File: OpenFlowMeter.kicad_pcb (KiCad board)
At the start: 2 copper layers, 74.5 x 28 mm, 101 parts, among them J1 Screw_Terminal_01x02, J2 Screw_Terminal_01x02, J3 Conn_01x06, J4 Conn_02x03_Odd_Even, J5 Conn_01x03, J6 Conn_02x04_Odd_Even, J7 Conn_02x03_Odd_Even, Q1 BC856, Q2 BC856, U1 LT1492, U2 STM32F103C8Tx, U3 LT1492, U4 R-78C3.3-1.0, U5 SN65HVD231, U6 LT1492, U7 24LC64, Y1 12 MHz

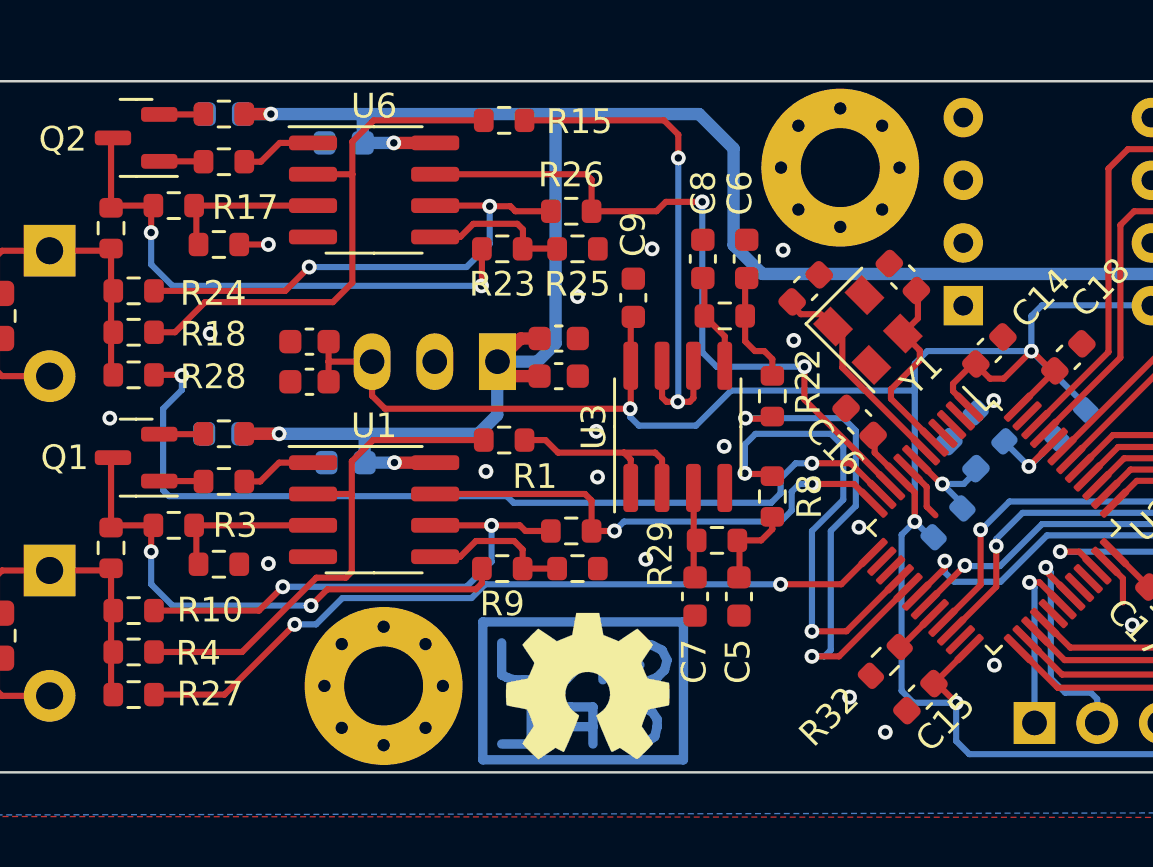
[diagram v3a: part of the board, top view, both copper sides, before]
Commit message: added ADC protection
added Zener diodes as ADC input protection in combination with current limiting resistors.
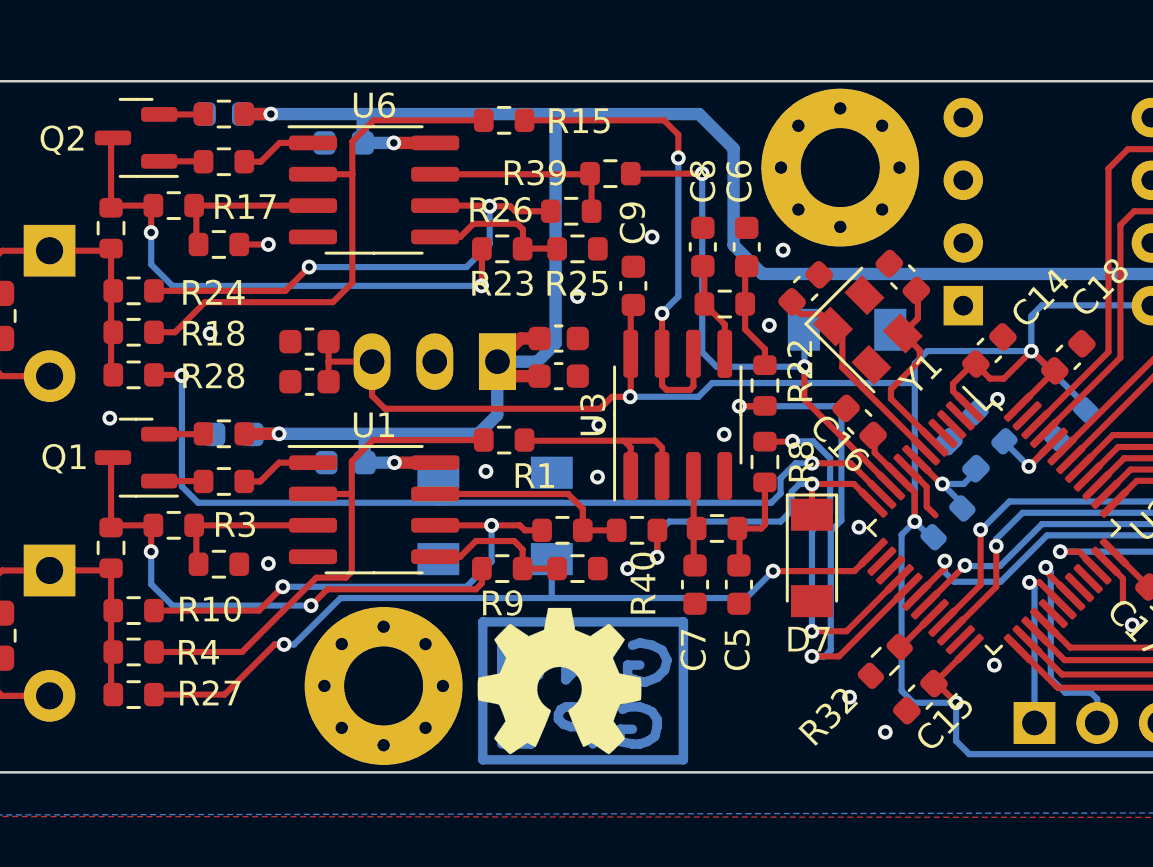
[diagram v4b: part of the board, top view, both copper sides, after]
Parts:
- added D5: 3V3, Diode_SMD:D_MiniMELF, B.Cu at (152.9, 92.8)
- added D6: 3V3, Diode_SMD:D_MiniMELF, B.Cu at (136.3, 100.4)
- added D7: 3V3, Diode_SMD:D_MiniMELF, F.Cu at (151.5, 102.1)
- added D8: 3V3, Diode_SMD:D_MiniMELF, B.Cu at (140.9, 100.4)
- added R39: 1k, Resistor_SMD:R_0603_1608Metric, F.Cu at (143.3, 86.5)
- added R40: 1k, Resistor_SMD:R_0603_1608Metric, F.Cu at (144.4, 101.0)
- C5, C6, C7, C8, C9: value C -> 100n
- moved R8 1.43 mm to (149.6, 98.2)
- moved REF** 1.16 mm to (141.3, 107.1)
- moved R22 0.53 mm to (149.6, 95.1)
- moved C6 0.48 mm to (148.8, 89.5)
- moved C8 0.48 mm to (147.1, 89.5)
- moved C9 0.48 mm to (144.2, 91.1)
- moved R30 0.48 mm to (148.0, 91.8)
- moved U3 0.48 mm to (146.1, 96.3)
- moved C5 0.48 mm to (148.5, 103.2)
- moved C7 0.48 mm to (146.8, 103.2)
- moved R29 0.48 mm to (147.6, 100.9)
- moved C1 0.41 mm to (128.0, 97.1)
- moved R12 0.36 mm to (141.4, 101.0)
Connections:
- R12 pad 1: /I1 -> Net-(R12-Pad1)
- R26 pad 1: /I2 -> Net-(R26-Pad1)
- U1 pad 7: /I1 -> Net-(R12-Pad1)
- U6 pad 7: /I2 -> Net-(R26-Pad1)
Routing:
- net Net-(R12-Pad1): track 0.00 -> 8.48 mm
- net Net-(R26-Pad1): track 0.00 -> 7.40 mm
- net /I1: track 20.6 -> 13.7 mm
- net /I2: track 29.1 -> 22.3 mm
- net /PWM1: track 19.1 -> 14.7 mm
- net /ISET 2: track 21.3 -> 19.6 mm
- net /U1: track 31.4 -> 33.0 mm
- net Net-(C5-Pad1): track 3.66 -> 4.45 mm
- net +3V3: track 160.6 -> 159.9 mm
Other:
- board text added: "Open FlowMeter"
- board text added: "v1.0"
- board text removed: "OpenFlowMeter"

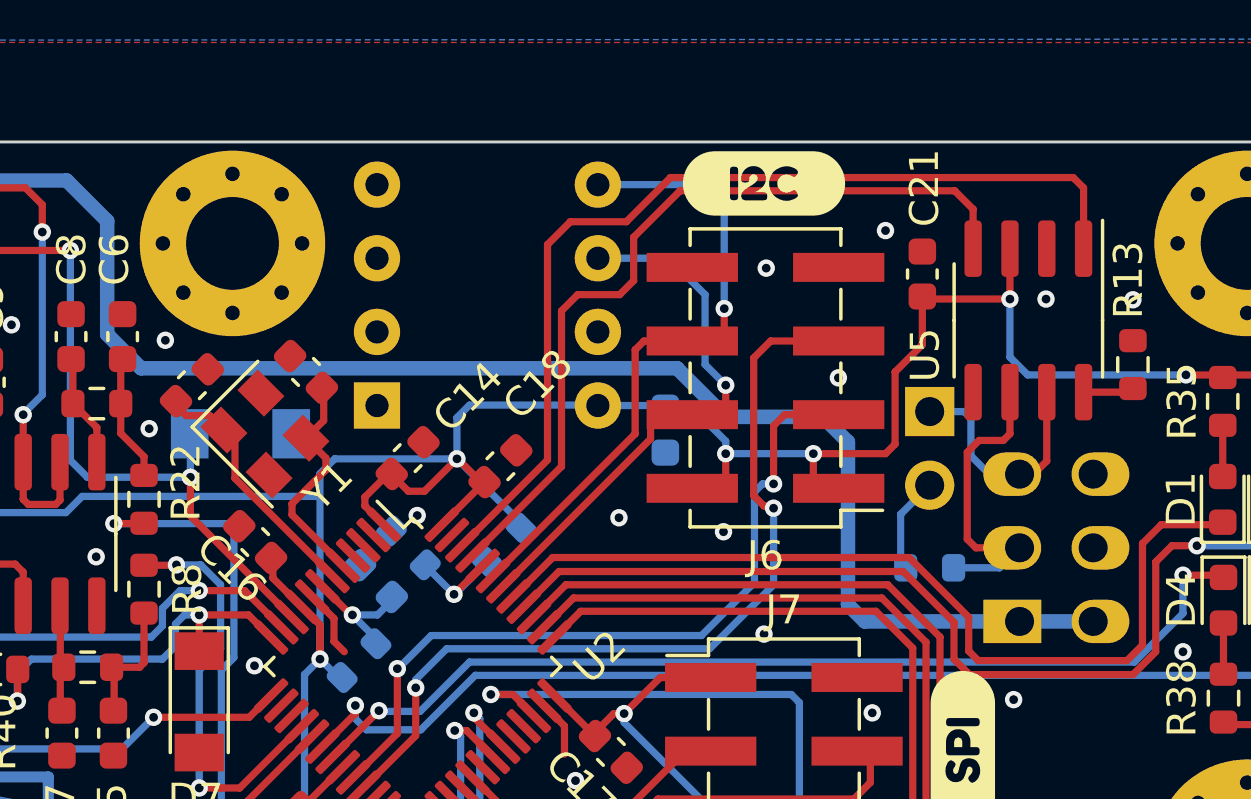
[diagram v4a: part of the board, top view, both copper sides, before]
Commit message: added write protection to EEPROM
added jumper, which can be opened and then the EEPROM is write protected.
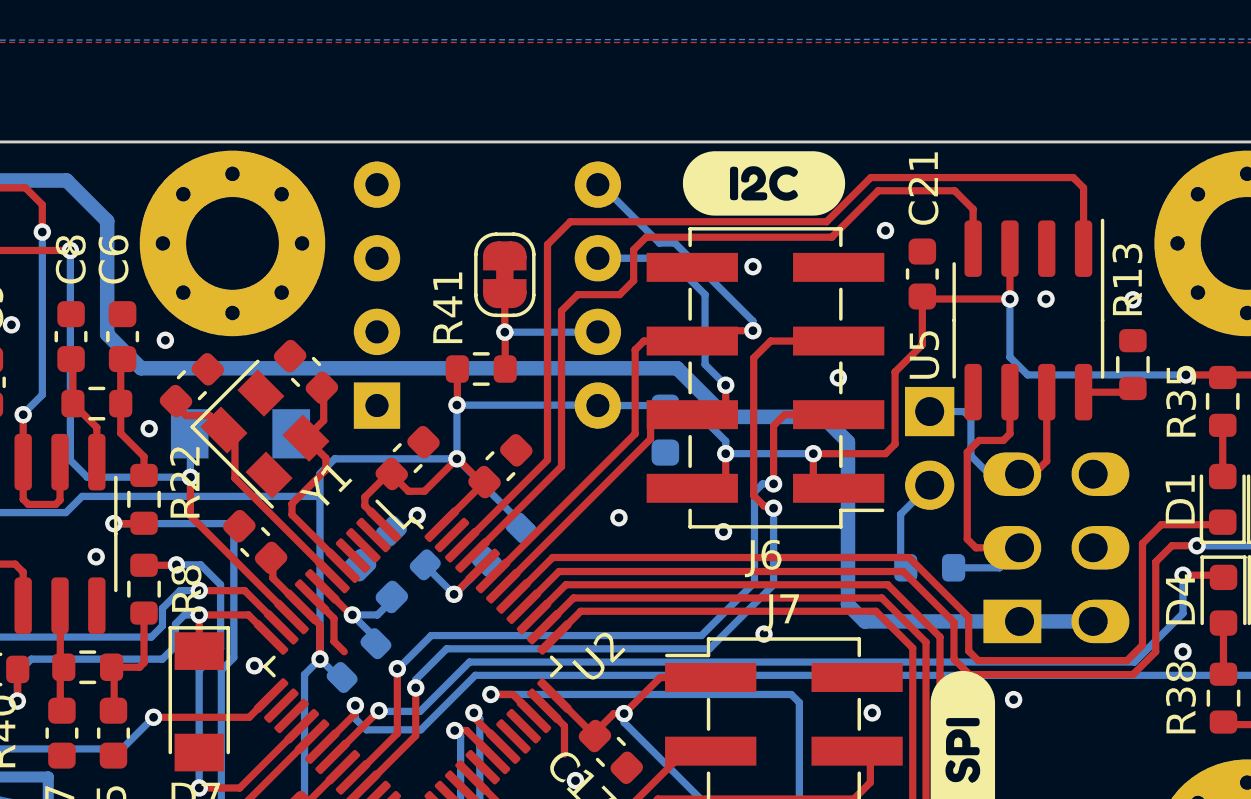
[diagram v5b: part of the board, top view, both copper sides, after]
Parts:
- added JP2: Jumper_2_Bridged, Jumper:SolderJumper-2_P1.3mm_Bridged_RoundedPad1.0x1.5mm, F.Cu at (162.0, 87.4)
- added R41: 10k, Resistor_SMD:R_0603_1608Metric, F.Cu at (161.2, 90.6)
- C1, C2, C3, C4: value C -> 100n
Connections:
- U7 pad 7: GND -> Net-(JP2-Pad2)
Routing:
- net Net-(JP2-Pad2): track 0.00 -> 5.75 mm, vias 0 -> 1
- net +3V3: track 159.9 -> 161.4 mm, vias 11 -> 12

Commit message: Some minor cleanups
Removed DRCs and did some minor cleanups.
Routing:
- net GND: vias 30 -> 39
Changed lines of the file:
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@@
   (segment (start 161.974109 98.096845) (end 167.0582 93.012754) (width 0.25) (layer "F.Cu") (net 28))
   (via (at 169.649 91.1606) (size 0.6) (drill 0.3) (layers "F.Cu" "B.Cu") (net 28))
-  (segment (start 169.649 91.1606) (end 168.9378 90.4494) (width 0.25) (layer "B.Cu") (net 28))
-  (segment (start 168.9378 88.0364) (end 167.6832 86.7818) (width 0.25) (layer "B.Cu") (net 28))
+  (segment (start 168.252 87.3506) (end 167.6832 86.7818) (width 0.25) (layer "B.Cu") (net 28))
   (segment (start 167.6832 86.7818) (end 165.2394 86.7818) (width 0.25) (layer "B.Cu") (net 28))
-  (segment (start 168.9378 90.4494) (end 168.9378 88.0364) (width 0.25) (layer "B.Cu") (net 28))
+  (segment (start 169.649 91.1606) (end 168.252 89.7636) (width 0.25) (layer "B.Cu") (net 28))
+  (segment (start 168.252 89.7636) (end 168.252 87.3506) (width 0.25) (layer "B.Cu") (net 28))
   (segment (start 155.733891 98.098891) (end 156.7204 99.0854) (width 0.25) (layer "F.Cu") (net 29))
   (segment (start 156.7204 99.0854) (end 156.7712 99.0854) (width 0.25) (layer "F.Cu") (net 29))
@@
   (segment (start 161.013 101.1682) (end 188.8006 101.1682) (width 0.25) (layer "B.Cu") (net 30))
   (segment (start 156.8728 102.2096) (end 156.8728 102.6668) (width 0.25) (layer "B.Cu") (net 30))
+  (segment (start 169.649 89.2048) (end 169.2172 89.6366) (width 0.25) (layer "F.Cu") (net 33))
   (segment (start 161.620555 97.741245) (end 166.5248 92.837) (width 0.25) (layer "F.Cu") (net 33))
   (segment (start 166.5248 89.9414) (end 166.8296 89.6366) (width 0.25) (layer "F.Cu") (net 33))
   (segment (start 166.5248 92.837) (end 166.5248 89.9414) (width 0.25) (layer "F.Cu") (net 33))
   (segment (start 166.8296 89.6366) (end 168.4956 89.6366) (width 0.25) (layer "F.Cu") (net 33))
-  (segment (start 169.5728 89.281) (end 169.2172 89.6366) (width 0.25) (layer "F.Cu") (net 33))
-  (segment (start 170.5888 89.281) (end 169.5728 89.281) (width 0.25) (layer "F.Cu") (net 33))
-  (via (at 170.5888 89.281) (size 0.6) (drill 0.3) (layers "F.Cu" "B.Cu") (net 33))
-  (segment (start 170.5888 89.281) (end 170.5888 88.9508) (width 0.25) (layer "B.Cu") (net 33))
-  (segment (start 165.3464 84.2418) (end 165.2394 84.2418) (width 0.25) (layer "B.Cu") (net 33))
-  (segment (start 170.5888 88.9508) (end 167.8964 86.2584) (width 0.25) (layer "B.Cu") (net 33))
-  (segment (start 167.363 86.2584) (end 165.3464 84.2418) (width 0.25) (layer "B.Cu") (net 33))
-  (segment (start 167.8964 86.2584) (end 167.363 86.2584) (width 0.25) (layer "B.Cu") (net 33))
+  (segment (start 169.649 88.6714) (end 169.649 89.2048) (width 0.25) (layer "F.Cu") (net 33))
+  (via (at 169.649 88.6714) (size 0.6) (drill 0.3) (layers "F.Cu" "B.Cu") (net 33))
+  (segment (start 169.649 84.9884) (end 169.649 88.6714) (width 0.25) (layer "B.Cu") (net 33))
+  (segment (start 168.9024 84.2418) (end 169.649 84.9884) (width 0.25) (layer "B.Cu") (net 33))
+  (segment (start 165.2394 84.2418) (end 168.9024 84.2418) (width 0.25) (layer "B.Cu") (net 33))
   (segment (start 163.9848 88.5952) (end 164.5436 88.0364) (width 0.25) (layer "F.Cu") (net 34))
   (segment (start 166.474 87.5538) (end 166.474 86.487) (width 0.25) (layer "F.Cu") (net 34))
@@
   (segment (start 145.5936 95.2738) (end 146.5366 95.2738) (width 0.25) (layer "F.Cu") (net 37))
   (segment (start 146.074 84.9338) (end 145.4936 84.3534) (width 0.25) (layer "F.Cu") (net 37))
-  (segment (start 146.074 85.8774) (end 146.074 84.9338) (width 0.25) (layer "F.Cu") (net 37))
+  (segment (start 145.4936 84.3534) (end 139.8416 84.3534) (width 0.25) (layer "F.Cu") (net 37))
   (segment (start 145.5936 95.2738) (end 145.4155 95.0957) (width 0.25) (layer "F.Cu") (net 37))
   (segment (start 145.4155 95.0957) (end 145.4155 93.8148) (width 0.25) (layer "F.Cu") (net 37))
+  (segment (start 146.074 84.9884) (end 146.074 84.9338) (width 0.25) (layer "F.Cu") (net 37))
   (segment (start 146.5366 95.2738) (end 146.6855 95.1249) (width 0.25) (layer "F.Cu") (net 37))
   (segment (start 146.6855 95.1249) (end 146.6855 93.8148) (width 0.25) (layer "F.Cu") (net 37))
-  (segment (start 145.4936 84.3534) (end 139.8416 84.3534) (width 0.25) (layer "F.Cu") (net 37))
   (segment (start 145.4155 93.8148) (end 145.4155 92.1785) (width 0.25) (layer "F.Cu") (net 37))
   (via (at 145.4155 92.1785) (size 0.6) (drill 0.3) (layers "F.Cu" "B.Cu") (net 37))
-  (via (at 146.074 85.8774) (size 0.6) (drill 0.3) (layers "F.Cu" "B.Cu") (net 37))
-  (segment (start 145.4155 92.1531) (end 146.074 91.4946) (width 0.25) (layer "B.Cu") (net 37))
-  (segment (start 145.4155 92.1785) (end 145.4155 92.1531) (width 0.25) (layer "B.Cu") (net 37))
-  (segment (start 146.074 91.4946) (end 146.074 85.8774) (width 0.25) (layer "B.Cu") (net 37))
+  (via (at 146.074 84.9884) (size 0.6) (drill 0.3) (layers "F.Cu" "B.Cu") (net 37))
+  (segment (start 145.4155 92.1531) (end 145.4155 92.1785) (width 0.25) (layer "B.Cu") (net 37))
+  (segment (start 146.074 91.4946) (end 145.4155 92.1531) (width 0.25) (layer "B.Cu") (net 37))
+  (segment (start 146.074 84.9884) (end 146.074 91.4946) (width 0.25) (layer "B.Cu") (net 37))
   (segment (start 118.468 93.0383) (end 118.468 94.5134) (width 0.25) (layer "F.Cu") (net 40))
   (segment (start 118.468 94.5134) (end 118.6712 94.7166) (width 0.25) (layer "F.Cu") (net 40))
@@
   (via (at 169.5728 96.2152) (size 0.6) (drill 0.3) (layers "F.Cu" "B.Cu") (free) (net 40))
   (via (at 142.852 96.6978) (size 0.6) (drill 0.3) (layers "F.Cu" "B.Cu") (free) (net 40))
+  (via (at 134.216 99.2124) (size 0.6) (drill 0.3) (layers "F.Cu" "B.Cu") (free) (net 40))
+  (via (at 138.153 85.6234) (size 0.6) (drill 0.3) (layers "F.Cu" "B.Cu") (free) (net 40))
   (via (at 129.4662 89.3826) (size 0.6) (drill 0.3) (layers "F.Cu" "B.Cu") (net 40))
   (via (at 147.932 97.0788) (size 0.6) (drill 0.3) (layers "F.Cu" "B.Cu") (free) (net 40))
+  (via (at 171.554 90.9574) (size 0.6) (drill 0.3) (layers "F.Cu" "B.Cu") (free) (net 40))
   (via (at 138.28 98.5774) (size 0.6) (drill 0.3) (layers "F.Cu" "B.Cu") (free) (net 40))
   (via (at 179.5804 102.0064) (size 0.6) (drill 0.3) (layers "F.Cu" "B.Cu") (free) (net 40))
   (via (at 173.5352 90.9066) (size 0.6) (drill 0.3) (layers "F.Cu" "B.Cu") (free) (net 40))
+  (via (at 119.23 98.5774) (size 0.6) (drill 0.3) (layers "F.Cu" "B.Cu") (free) (net 40))
   (via (at 159.0064 95.6564) (size 0.6) (drill 0.3) (layers "F.Cu" "B.Cu") (free) (net 40))
   (via (at 154.4598 109.1438) (size 0.6) (drill 0.3) (layers "F.Cu" "B.Cu") (free) (net 40))
   (via (at 185.4224 100.3554) (size 0.6) (drill 0.3) (layers "F.Cu" "B.Cu") (free) (net 40))
   (via (at 158.8794 106.426) (size 0.6) (drill 0.3) (layers "F.Cu" "B.Cu") (free) (net 40))
-  (via (at 170.5888 87.0712) (size 0.6) (drill 0.3) (layers "F.Cu" "B.Cu") (free) (net 40))
-  (via (at 165.966 95.7326) (size 0.6) (drill 0.3) (layers "F.Cu" "B.Cu") (free) (net 40))
+  (via (at 171.046 87.0712) (size 0.6) (drill 0.3) (layers "F.Cu" "B.Cu") (free) (net 40))
+  (via (at 165.966 96.2152) (size 0.6) (drill 0.3) (layers "F.Cu" "B.Cu") (free) (net 40))
   (via (at 153.012 107.7214) (size 0.6) (drill 0.3) (layers "F.Cu" "B.Cu") (free) (net 40))
   (via (at 175.1608 85.8266) (size 0.6) (drill 0.3) (layers "F.Cu" "B.Cu") (free) (net 40))
   (via (at 127.104 92.9894) (size 0.6) (drill 0.3) (layers "F.Cu" "B.Cu") (free) (net 40))
+  (via (at 134.216 102.0064) (size 0.6) (drill 0.3) (layers "F.Cu" "B.Cu") (free) (net 40))
   (via (at 142.8012 98.806) (size 0.6) (drill 0.3) (layers "F.Cu" "B.Cu") (free) (net 40))
+  (via (at 134.089 86.5124) (size 0.6) (drill 0.3) (layers "F.Cu" "B.Cu") (free) (net 40))
   (via (at 149.7608 92.6592) (size 0.6) (drill 0.3) (layers "F.Cu" "B.Cu") (free) (net 40))
   (via (at 170.9698 99.7458) (size 0.6) (drill 0.3) (layers "F.Cu" "B.Cu") (free) (net 40))
@@
   (via (at 153.393 100.838) (size 0.6) (drill 0.3) (layers "F.Cu" "B.Cu") (free) (net 40))
   (via (at 145.011 89.0778) (size 0.6) (drill 0.3) (layers "F.Cu" "B.Cu") (free) (net 40))
+  (via (at 134.089 88.6714) (size 0.6) (drill 0.3) (layers "F.Cu" "B.Cu") (free) (net 40))
+  (via (at 117.96 98.5774) (size 0.6) (drill 0.3) (layers "F.Cu" "B.Cu") (free) (net 40))
   (via (at 164.4674 104.8004) (size 0.6) (drill 0.3) (layers "F.Cu" "B.Cu") (free) (net 40))
+  (via (at 166.982 88.2904) (size 0.6) (drill 0.3) (layers "F.Cu" "B.Cu") (free) (net 40))
   (via (at 174.7036 102.4636) (size 0.6) (drill 0.3) (layers "F.Cu" "B.Cu") (free) (net 40))
   (via (at 180.698 88.1888) (size 0.6) (drill 0.3) (layers "F.Cu" "B.Cu") (free) (net 40))
